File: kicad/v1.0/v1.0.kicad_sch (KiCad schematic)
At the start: 50 parts, among them J1 USB_B_Micro, J2 9V_IN, J3 MOTOR, J4 LED, J5 BUTTON, Q1 IRF520, SW1 RESET, SW2 FLASH, U1 MCP2221AxSL, U2 MAX14872ETC+, U3 ESP32-WROOM-32, U6 AZ1117-3.3

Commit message: getting ready to start designing PCB 1.0
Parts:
- removed R7: 10k, Resistor_SMD:R_0805_2012Metric_Pad1.20x1.40mm_HandSolder, symbol Device:R
- removed U2: MAX14872ETC+, MAX14872ETC_:SON50P300X300X80-13N, symbol MAX14872ETC_:MAX14872ETC+
- added C15: 22u, Capacitor_SMD:C_0805_2012Metric_Pad1.18x1.45mm_HandSolder, symbol Device:C
- added R10: 1k, Resistor_SMD:R_0805_2012Metric_Pad1.20x1.40mm_HandSolder, symbol Device:R
- added U2: ZXBM5210-SP, Package_SO:Diodes_SO-8EP, symbol Driver_Motor:ZXBM5210-SP
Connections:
- net SNS is gone; now on net +9V: R1.1
- net +9V: now also U2.3 (VDD), U2.6 (VREF)
- net FWD: now also U2.4 (FWD)
- net GND: now also C15.2, U2.8 (GND), U2.9 (GND)
- net REV: now also U2.5 (REV)
- net at U3.25 (IO0): now also R10.1; no longer SW2.1
- net at J3.1 (Pin_1): now also U2.7 (OUT2)
- net at J3.2 (Pin_2): now also U2.1 (OUT1)
- new net: R10.2, SW2.1
- new net: C15.1, U2.2 (VM)
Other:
- moved on the sheet: C1, C12, C13, C14, C4, C8, J3, SW2, TP2, TP3

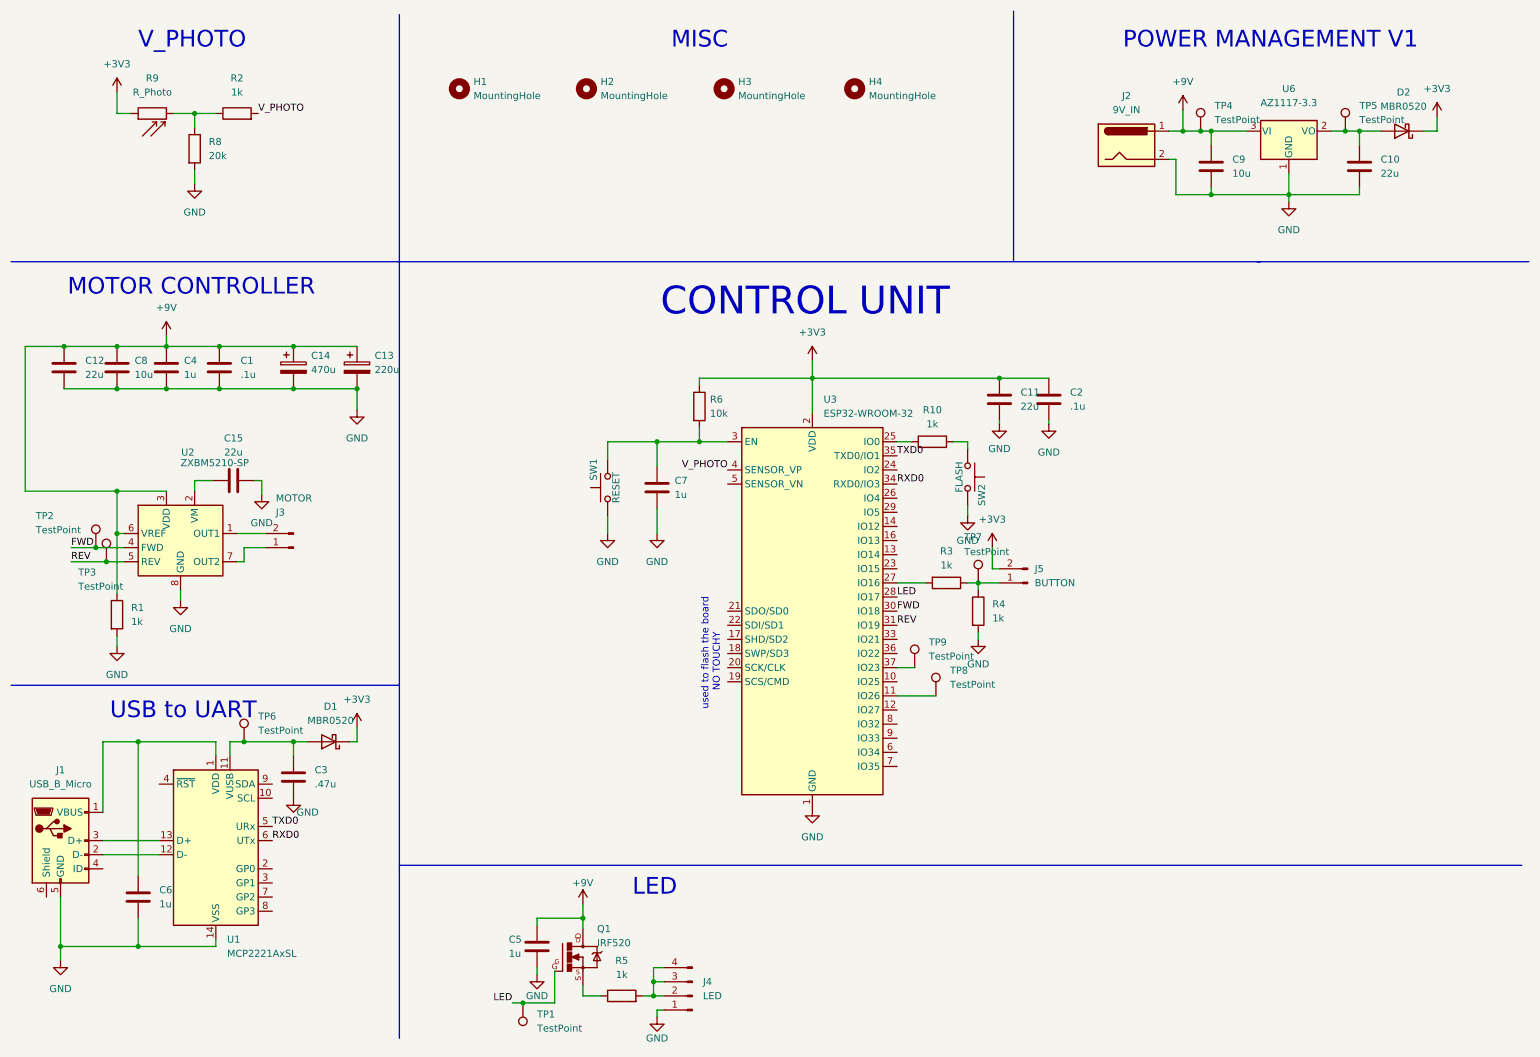
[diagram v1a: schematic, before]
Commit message: PCB v1.0 is designed and sent to Nikhil, don't modify anything in here anymore
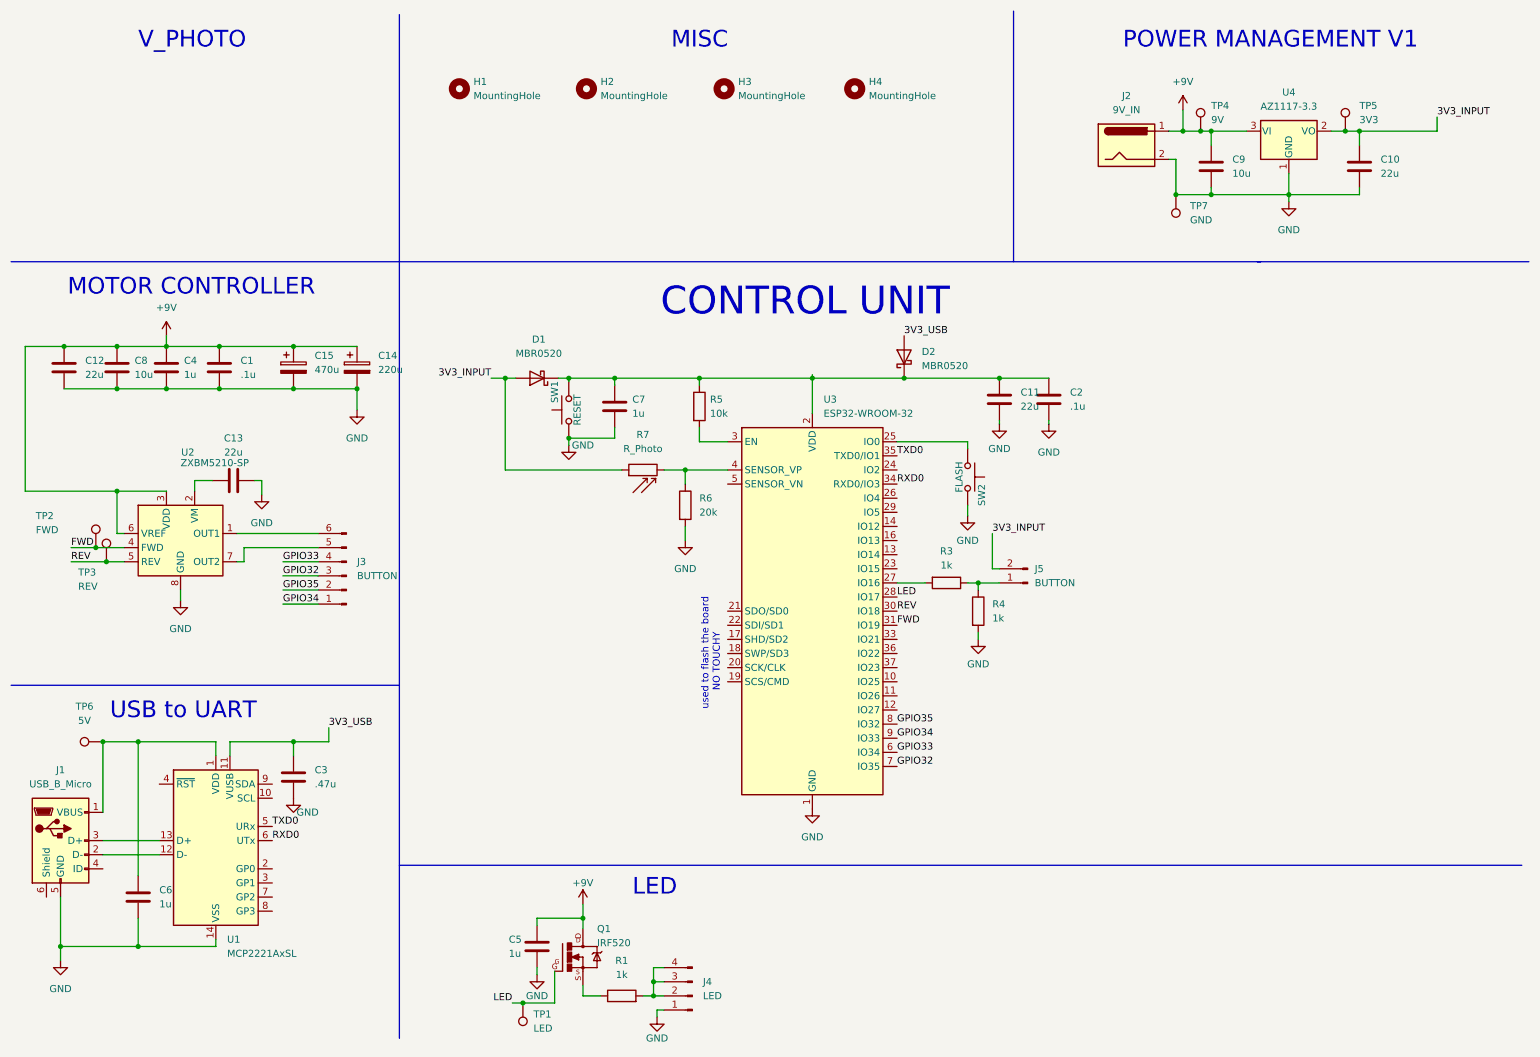
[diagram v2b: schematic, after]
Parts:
- removed J3: MOTOR, Connector_Molex:Molex_KK-254_AE-6410-02A_1x02_P2.54mm_Vertical, symbol Connector:Conn_01x02_Male
- removed R1, R10, R2: 1k, Resistor_SMD:R_0805_2012Metric_Pad1.20x1.40mm_HandSolder, symbol Device:R
- removed TP8, TP9: TestPoint, TestPoint:TestPoint_Pad_2.5x2.5mm, symbol Connector:TestPoint
- added J3: BUTTON, Connector_Molex:Molex_KK-254_AE-6410-06A_1x06_P2.54mm_Vertical, symbol Connector:Conn_01x06_Male
- SW1, SW2: footprint Button_Switch_THT:SW_PUSH-12mm_Wuerth-430476085716 -> Button_Switch_THT:SW_PUSH_6mm
- TP1: value TestPoint -> LED
- TP2: value TestPoint -> FWD
- TP3: value TestPoint -> REV
- TP4: value TestPoint -> 9V
- TP5: value TestPoint -> 3V3
- TP6: value TestPoint -> 5V
- TP7: value TestPoint -> GND
- U4: renamed from U6; footprint Package_TO_SOT_SMD:SOT-223 -> Package_TO_SOT_SMD:SOT-89-3_Handsoldering
- renumbered C15 to C13, C13 to C14, C14 to C15, D2 to D1, D1 to D2, R5 to R1, R6 to R5, R8 to R6, R9 to R7
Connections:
- net V_PHOTO is gone; now on an unnamed net: U3.4 (SENSOR_VP)
- net FWD: now also U3.31 (IO19); no longer U3.30 (IO18)
- net GND: now also TP7.1
- net REV: now also U3.30 (IO18); no longer U3.31 (IO19)
- net 3V3_INPUT: now reaches C10.1, D1.2 (A), TP5.1, U4.2 (VO)
- net 3V3_INPUT: now also J5.2 (Pin_2), R7.1
- net at U3.25 (IO0): now also SW2.1
- net 3V3_USB: now reaches C3.1, D2.2 (A), U1.11 (VUSB)
- net 3V3_USB: no longer TP6.1
- net at C6.1, J1.1 (VBUS), U1.1 (VDD): now also TP6.1
- net at U2.7 (OUT2): now also J3.5 (Pin_5)
- net at U2.1 (OUT1): now also J3.6 (Pin_6)
- net at C7.1, SW1.2: now also C11.1, C2.1, D1.1 (K), D2.1 (K), R5.1, U3.2 (VDD); no longer R5.2, U3.3 (EN)
- net at J5.1 (Pin_1), R3.1, R4.1: no longer TP7.1
- net GPIO33: now reaches U3.6 (IO34)
- net GPIO33: now also J3.4 (Pin_4)
- net GPIO32: now reaches U3.7 (IO35)
- net GPIO32: now also J3.3 (Pin_3)
- net GPIO35: now reaches U3.8 (IO32)
- net GPIO35: now also J3.2 (Pin_2)
- net GPIO34: now reaches U3.9 (IO33)
- net GPIO34: now also J3.1 (Pin_1)
- removed net +3V3: C11.1, C2.1, D1.1 (K), D2.1 (K), J5.2 (Pin_2), R5.1, R7.1, U3.2 (VDD)
- new net: R5.2, U3.3 (EN)
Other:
- moved on the sheet: C7, D1, D2, R6, R7, SW1
